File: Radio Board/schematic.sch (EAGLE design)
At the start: 13 parts, among them J1 132134RP

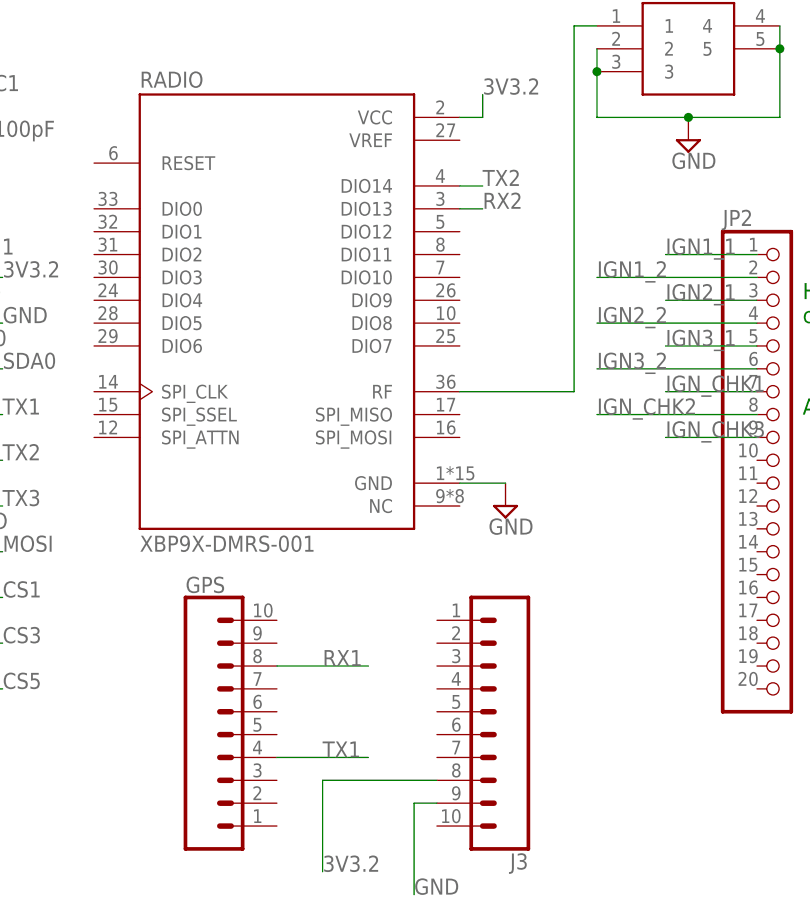
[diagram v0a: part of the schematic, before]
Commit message: fixed wiring on radio board
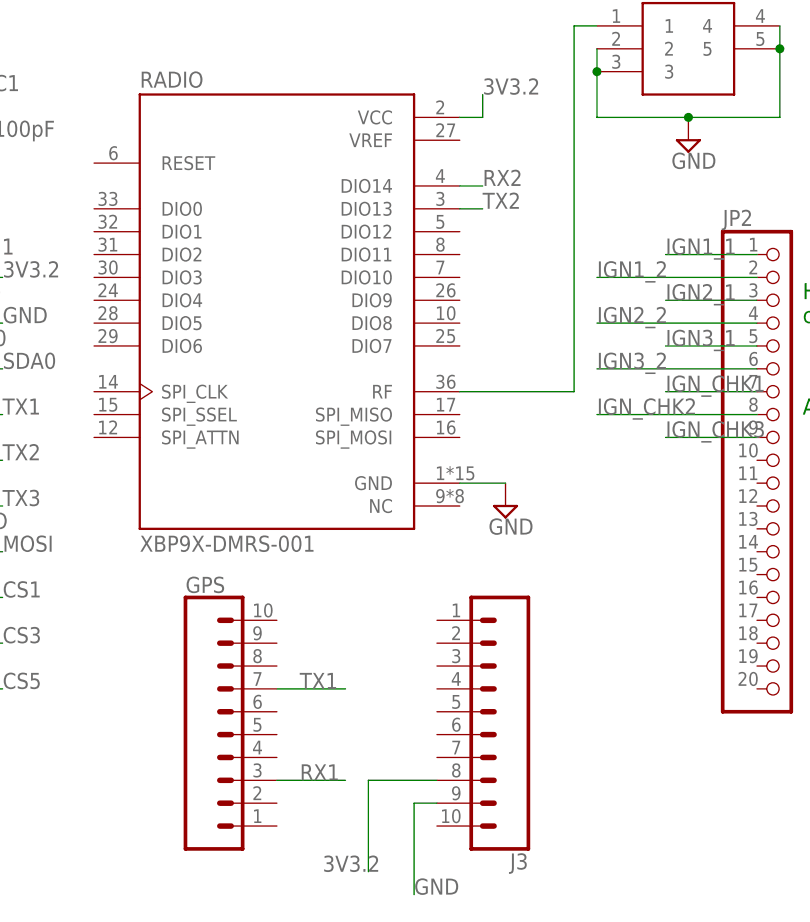
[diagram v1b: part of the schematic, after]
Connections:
- net RX1: now also GPS.3; no longer GPS.8
- net RX2: now also RADIO.DIO14; no longer RADIO.DIO13
- net TX1: now also GPS.7; no longer GPS.4
- net TX2: now also RADIO.DIO13; no longer RADIO.DIO14
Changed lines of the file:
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@@
 <segment>
 <pinref part="J3" gate="J1" pin="8"/>
-<wire x1="66.04" y1="-7.62" x2="53.34" y2="-7.62" width="0.1524" layer="91"/>
-<wire x1="53.34" y1="-7.62" x2="53.34" y2="-17.78" width="0.1524" layer="91"/>
+<wire x1="66.04" y1="-7.62" x2="58.42" y2="-7.62" width="0.1524" layer="91"/>
+<wire x1="58.42" y1="-7.62" x2="58.42" y2="-17.78" width="0.1524" layer="91"/>
 <label x="53.34" y="-17.78" size="1.778" layer="95"/>
 </segment>
@@
 </segment>
 <segment>
-<wire x1="48.26" y1="5.08" x2="58.42" y2="5.08" width="0.1524" layer="91"/>
-<label x="53.34" y="5.08" size="1.778" layer="95"/>
-<pinref part="GPS" gate="J1" pin="8"/>
+<pinref part="GPS" gate="J1" pin="3"/>
+<wire x1="48.26" y1="-7.62" x2="55.88" y2="-7.62" width="0.1524" layer="91"/>
+<label x="50.8" y="-7.62" size="1.778" layer="95"/>
 </segment>
 </net>
@@
 </segment>
 <segment>
-<wire x1="48.26" y1="-5.08" x2="58.42" y2="-5.08" width="0.1524" layer="91"/>
-<label x="53.34" y="-5.08" size="1.778" layer="95"/>
-<pinref part="GPS" gate="J1" pin="4"/>
+<pinref part="GPS" gate="J1" pin="7"/>
+<wire x1="48.26" y1="2.54" x2="55.88" y2="2.54" width="0.1524" layer="91"/>
+<label x="50.8" y="2.54" size="1.778" layer="95"/>
 </segment>
 </net>
@@
 </segment>
 <segment>
-<pinref part="RADIO" gate="G$1" pin="DIO13"/>
-<wire x1="68.58" y1="55.88" x2="71.12" y2="55.88" width="0.1524" layer="91"/>
-<label x="71.12" y="55.88" size="1.778" layer="95"/>
+<pinref part="RADIO" gate="G$1" pin="DIO14"/>
+<wire x1="68.58" y1="58.42" x2="71.12" y2="58.42" width="0.1524" layer="91"/>
+<label x="71.12" y="58.42" size="1.778" layer="95"/>
 </segment>
 </net>
@@
 </segment>
 <segment>
-<pinref part="RADIO" gate="G$1" pin="DIO14"/>
-<wire x1="68.58" y1="58.42" x2="71.12" y2="58.42" width="0.1524" layer="91"/>
-<label x="71.12" y="58.42" size="1.778" layer="95"/>
+<pinref part="RADIO" gate="G$1" pin="DIO13"/>
+<wire x1="68.58" y1="55.88" x2="71.12" y2="55.88" width="0.1524" layer="91"/>
+<label x="71.12" y="55.88" size="1.778" layer="95"/>
 </segment>
 </net>
